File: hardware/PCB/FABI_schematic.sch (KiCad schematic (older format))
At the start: 9 parts

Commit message: Added first PCB draft
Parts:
- removed J? (x8): PJ-392, symbol Connector:AudioJack3
- added C1, C4: 10u, Capacitor_THT:C_Disc_D6.0mm_W4.4mm_P5.00mm, symbol Device:C
- added C11, C12: 100n, Capacitor_SMD:C_0805_2012Metric_Pad1.15x1.40mm_HandSolder, symbol Device:C
- added C13, C6: 10u, Capacitor_SMD:C_0805_2012Metric_Pad1.15x1.40mm_HandSolder, symbol Device:C
- added C14: 100u, Capacitor_Tantalum_SMD:CP_EIA-3216-12_Kemet-S_Pad1.58x1.35mm_HandSolder, symbol Device:CP
- added C2, C3: 100n, Capacitor_THT:C_Disc_D4.7mm_W2.5mm_P5.00mm, symbol Device:C
- added C5: 100u, Capacitor_THT:CP_Radial_D5.0mm_P2.00mm, symbol Device:CP
- added D1, D2, D3, D4, D5, D6, D7, D8: P6KE6.8A, Diode_THT:D_DO-201AE_P5.08mm_Vertical_KathodeUp, symbol Diode:1.5KExxA
- added D10: LED, LED_SMD:LED_0805_2012Metric_Pad1.15x1.40mm_HandSolder, symbol Device:LED
- added D11, D12: SP0504BAHT, Package_TO_SOT_SMD:SOT-23-5, symbol Power_Protection:SP0504BAHT
- added D9: LED, LED_THT:LED_D3.0mm, symbol Device:LED
- added J1, J2, J3, J4, J5, J6, J7, J8: PJ307, PJ307:PJ-307, symbol Connector:AudioJack3_SwitchTR
- added J9: Conn_01x06_Male, Connector_PinHeader_2.54mm:PinHeader_1x06_P2.54mm_Vertical, symbol Connector:Conn_01x06_Male
- added JP1: SolderJumper_2_Open, Jumper:SolderJumper-2_P1.3mm_Open_Pad1.0x1.5mm, symbol Jumper:SolderJumper_2_Open
- added R1, R5, R7: 10k, Resistor_THT:R_Axial_DIN0204_L3.6mm_D1.6mm_P7.62mm_Horizontal, symbol Device:R
- added R10: 330R, Resistor_SMD:R_0805_2012Metric_Pad1.15x1.40mm_HandSolder, symbol Device:R
- added R2: 18k, Resistor_THT:R_Axial_DIN0204_L3.6mm_D1.6mm_P7.62mm_Horizontal, symbol Device:R
- added R3, R6, R8: 10k, Resistor_SMD:R_0805_2012Metric_Pad1.15x1.40mm_HandSolder, symbol Device:R
- added R4: 18k, Resistor_SMD:R_0805_2012Metric_Pad1.15x1.40mm_HandSolder, symbol Device:R
- added R9: 330R, Resistor_THT:R_Axial_DIN0204_L3.6mm_D1.6mm_P7.62mm_Horizontal, symbol Device:R
- added SW1, SW3: SW_Push, Button_Switch_THT:SW_PUSH_6mm, symbol Switch:SW_Push
- added TP1, TP2, TP3, TP4, TP5, TP6: TestPoint, TestPoint:TestPoint_Pad_1.0x1.0mm, symbol Connector:TestPoint
- added U1: LD1117V33-DG, Package_TO_SOT_THT:TO-220-3_Vertical, symbol Regulator_Linear:AZ1117-3.3
- added U3: NCP1117-3.3_SOT223, Package_TO_SOT_SMD:SOT-223-3_TabPin2, symbol Regulator_Linear:NCP1117-3.3_SOT223
- added U4: ESP32-WROOM-32, RF_Module:ESP32-WROOM-32, symbol RF_Module:ESP32-WROOM-32
- U2: renamed from U?; footprint (none) -> ProMicro:ProMicro
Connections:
- net labels added: +3V3, 1, 2, 3, 4, 5, 6, 7, 8, A_RX, A_TX, EN, ESP_RX, IO0, LED, RXD0, TXD0, VCC
- wire segments 56 -> 76
- no-connect marks 23 -> 63
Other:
- note added: "SMD components"
- note added: "THT components"
- note removed: "(D2)"
- note removed: "(D3)"
- note removed: "(D4)"
- note removed: "(D5)"
- note removed: "(D6)"
- note removed: "(D7)"
- note removed: "(D8)"
- note removed: "(D9)"
- note removed: "1"
- note removed: "2"
- note removed: "3"
- note removed: "4"
- note removed: "5"
- note removed: "6"
- note removed: "7"
- note removed: "8"
- note removed: "Easiest way for assembly:\n1.) Mount the ProMicro in its position (with hot glue, only on unused pin header)\n2.) Solder enamelled wire on ProMicro (just one side, take care of sufficient length)\n3.) Mount the JackPlugs, fix with hot glue\n4.) Solder GND connection\n5.) Solder remaining signals\n6.) Stabilize the USB plug with hot glue (attach a cable, otherwise you may have glue IN the plug)."

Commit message: Removed ESP32 from FABI PCB, we will use the FM BT Addon. Added QR codes to UserManual & Releases
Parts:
- removed C1, C4: 10u, Capacitor_THT:C_Disc_D6.0mm_W4.4mm_P5.00mm, symbol Device:C
- removed C11, C12: 100n, Capacitor_SMD:C_0805_2012Metric_Pad1.15x1.40mm_HandSolder, symbol Device:C
- removed C13, C6: 10u, Capacitor_SMD:C_0805_2012Metric_Pad1.15x1.40mm_HandSolder, symbol Device:C
- removed C14: 100u, Capacitor_Tantalum_SMD:CP_EIA-3216-12_Kemet-S_Pad1.58x1.35mm_HandSolder, symbol Device:CP
- removed C2, C3: 100n, Capacitor_THT:C_Disc_D4.7mm_W2.5mm_P5.00mm, symbol Device:C
- removed C5: 100u, Capacitor_THT:CP_Radial_D5.0mm_P2.00mm, symbol Device:CP
- removed D10: LED, LED_SMD:LED_0805_2012Metric_Pad1.15x1.40mm_HandSolder, symbol Device:LED
- removed D9: LED, LED_THT:LED_D3.0mm, symbol Device:LED
- removed J9: Conn_01x06_Male, Connector_PinHeader_2.54mm:PinHeader_1x06_P2.54mm_Vertical, symbol Connector:Conn_01x06_Male
- removed JP1: SolderJumper_2_Open, Jumper:SolderJumper-2_P1.3mm_Open_Pad1.0x1.5mm, symbol Jumper:SolderJumper_2_Open
- removed R10: 330R, Resistor_SMD:R_0805_2012Metric_Pad1.15x1.40mm_HandSolder, symbol Device:R
- removed R5, R7: 10k, Resistor_THT:R_Axial_DIN0204_L3.6mm_D1.6mm_P7.62mm_Horizontal, symbol Device:R
- removed R6, R8: 10k, Resistor_SMD:R_0805_2012Metric_Pad1.15x1.40mm_HandSolder, symbol Device:R
- removed R9: 330R, Resistor_THT:R_Axial_DIN0204_L3.6mm_D1.6mm_P7.62mm_Horizontal, symbol Device:R
- removed SW1, SW3: SW_Push, Button_Switch_THT:SW_PUSH_6mm, symbol Switch:SW_Push
- removed TP1, TP2, TP3, TP4, TP5, TP6: TestPoint, TestPoint:TestPoint_Pad_1.0x1.0mm, symbol Connector:TestPoint
- removed U1: LD1117V33-DG, Package_TO_SOT_THT:TO-220-3_Vertical, symbol Regulator_Linear:AZ1117-3.3
- removed U3: NCP1117-3.3_SOT223, Package_TO_SOT_SMD:SOT-223-3_TabPin2, symbol Regulator_Linear:NCP1117-3.3_SOT223
- removed U4: ESP32-WROOM-32, RF_Module:ESP32-WROOM-32, symbol RF_Module:ESP32-WROOM-32
- added J9: Conn_02x05_Odd_Even, Connector_PinHeader_2.54mm:PinHeader_2x05_P2.54mm_Vertical, symbol Connector_Generic:Conn_02x05_Odd_Even
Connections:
- net labels removed: +3V3, EN, IO0, LED, RXD0, TXD0
- wire segments 76 -> 37
- no-connect marks 63 -> 40

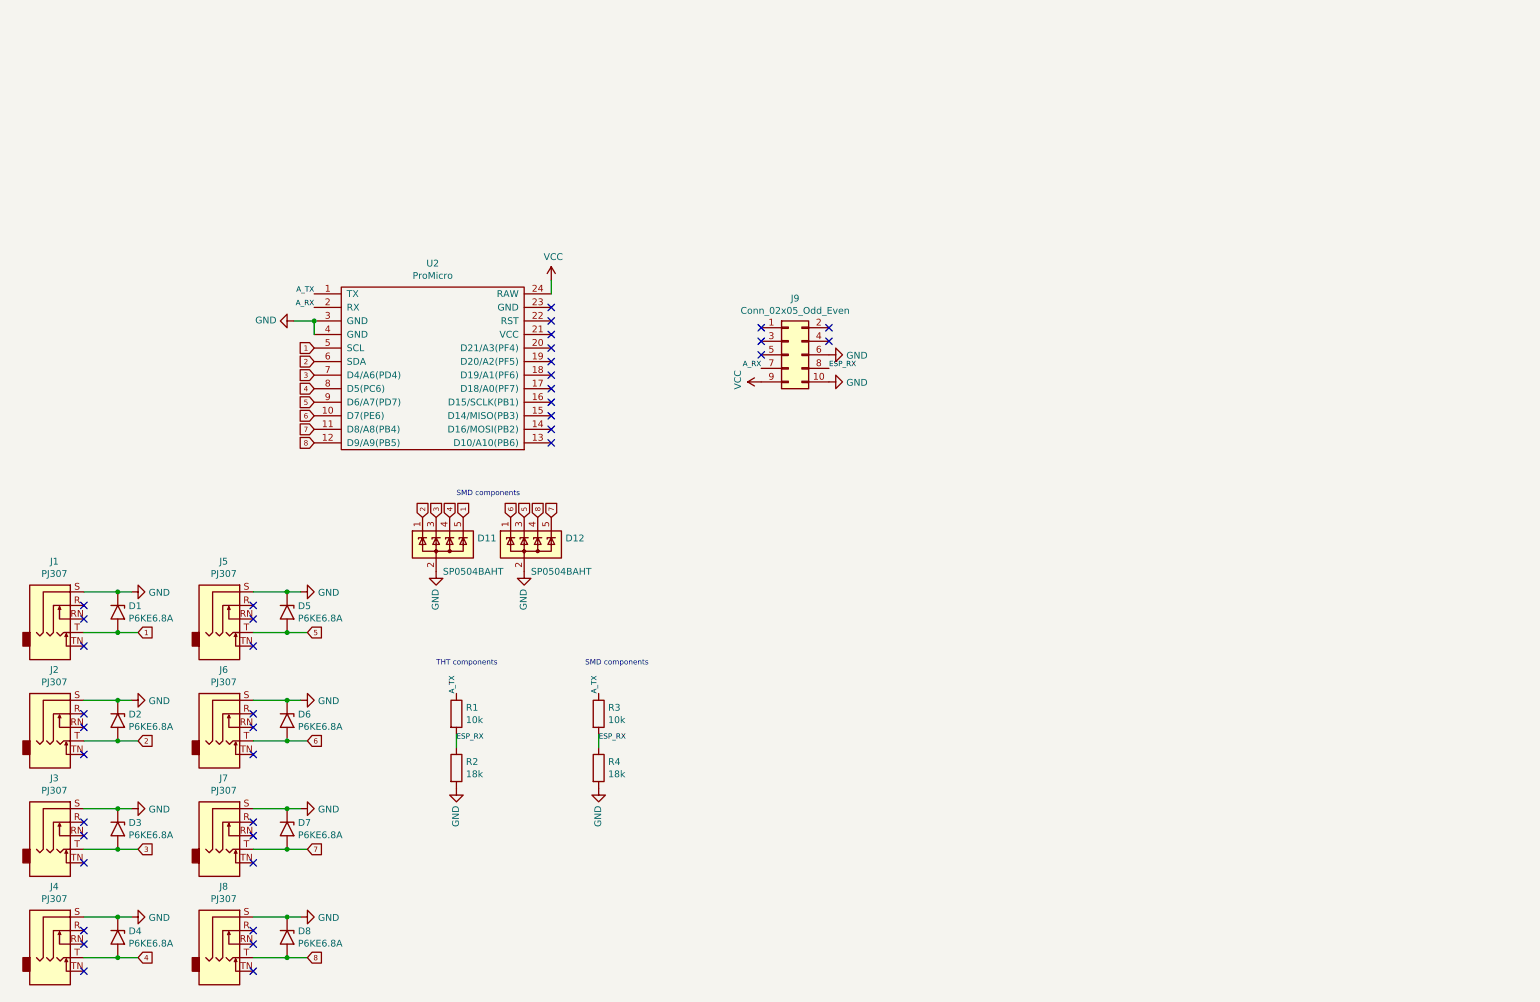
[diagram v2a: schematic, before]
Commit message: Added Neopixel & MPX pressure sensor to PCB.
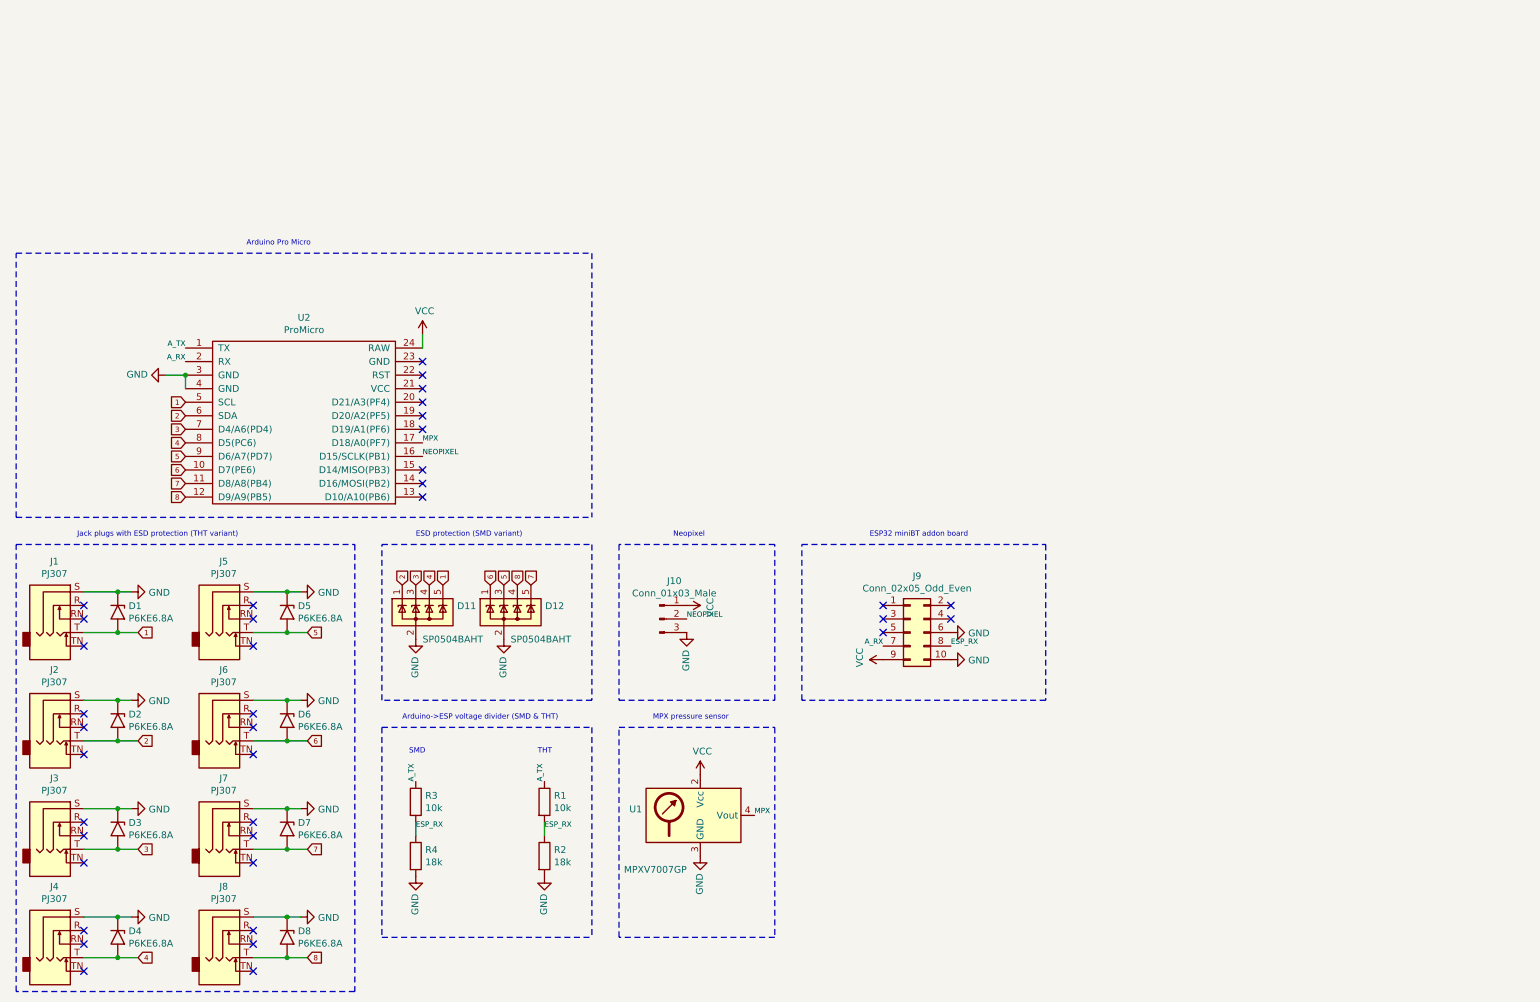
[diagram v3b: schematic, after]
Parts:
- added J10: Conn_01x03_Male, Connector_PinHeader_2.54mm:PinHeader_1x03_P2.54mm_Vertical, symbol Connector:Conn_01x03_Male
- added U1: MPXV7007GP, MPXV7007:MPXV7007GP, symbol Sensor_Pressure:MPXA6115A
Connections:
- net GND: now also J10.3 (Pin_3), U1.3 (GND)
- net VCC: now also J10.1 (Pin_1), U1.2 (Vcc)
- net NEOPIXEL: now reaches U2.16 (D15/SCLK(PB1))
- net NEOPIXEL: now also J10.2 (Pin_2)
- net MPX: now reaches U2.17 (D18/A0(PF7))
- net MPX: now also U1.4 (Vout)
- no-connect marks 40 -> 38
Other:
- note added: "Arduino Pro Micro"
- note added: "Arduino->ESP voltage divider (SMD & THT)"
- note added: "ESD protection (SMD variant)"
- note added: "ESP32 miniBT addon board"
- note added: "Jack plugs with ESD protection (THT variant)"
- note added: "MPX pressure sensor"
- note added: "Neopixel"
- note added: "SMD"
- note added: "THT"
- note removed: "SMD components"
- note removed: "THT components"
- moved on the sheet: D11, D12, J9, R1, R2, R3, R4, U2
